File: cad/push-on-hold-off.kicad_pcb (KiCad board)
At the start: 2 copper layers, 11 parts, among them P1 CONN_01X04, P2 CONN_01X04, Q1 IRF7309IPBF, SW1 SW_PUSH_SMALL

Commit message: Do some placing and draw outline
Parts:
- moved R4 11.4 mm to (226.4, 111.2), turned to 180 degrees
- moved P1 7.50 mm to (218.4, 110.5), turned to 180 degrees
- moved C2 4.81 mm to (231.3, 111.1), turned to 0 degrees
- moved P2 3.47 mm to (236.2, 102.9)
- moved R1 3.00 mm to (221.0, 106.0), turned to 270 degrees
- moved R3 2.24 mm to (232.0, 102.0)
- moved R2 2.00 mm to (223.0, 106.0)
- moved SW1 1.70 mm to (227.3, 106.7)
- moved D1 1.17 mm to (226.4, 102.0)
- moved C1 1.06 mm to (222.4, 102.0)
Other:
- board outline added: 22.9 x 12.7 mm
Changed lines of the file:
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@@
     (links 27)
     (no_connects 27)
-    (area 0 0 0 0)
+    (area 215.824999 100.254999 238.835001 113.105001)
     (thickness 1.6)
-    (drawings 0)
+    (drawings 8)
     (tracks 0)
     (zones 0)
@@
   (layers
     (0 F.Cu signal)
-    (31 B.Cu signal)
+    (31 B.Cu signal hide)
     (32 B.Adhes user)
     (33 F.Adhes user)
@@
     (pad_to_mask_clearance 0.2)
     (aux_axis_origin 0 0)
-    (visible_elements FFFFFF7F)
+    (visible_elements FFFF7F7F)
     (pcbplotparams
       (layerselection 0x00030_80000001)
@@
   )
   (module Capacitors_SMD.pretty:C_0603_HandSoldering (layer F.Cu)
-    (at 222 103 180)
+    (at 222.36 102 180)
     (descr "Capacitor SMD 0603, hand soldering")
     (tags "capacitor 0603")
     (attr smd)
-    (fp_text reference C1 (at 0 -1.9 180) (layer F.SilkS)
-      (effects (font (size 1 1) (thickness 0.15)))
-    )
-    (fp_text value 1uF (at 0 1.9 180) (layer F.Fab)
+    (fp_text reference C1 (at 0.07 -1.64 180) (layer F.SilkS)
+      (effects (font (size 1 1) (thickness 0.15)))
+    )
+    (fp_text value 1uF (at -0.1 -1.51 180) (layer F.Fab)
       (effects (font (size 1 1) (thickness 0.15)))
     )
@@
   )
   (module Diodes_SMD.pretty:SOD-323 (layer F.Cu)
-    (at 227 103)
+    (at 226.39 102)
     (descr SOD-323)
     (tags SOD-323)
     (attr smd)
-    (fp_text reference D1 (at 0 -1.85) (layer F.SilkS)
+    (fp_text reference D1 (at 0.03 1.65) (layer F.SilkS)
       (effects (font (size 1 1) (thickness 0.15)))
     )
@@
     (tags "SOIC 1.27")
     (attr smd)
-    (fp_text reference Q1 (at 0 -3.68) (layer F.SilkS)
-      (effects (font (size 1 1) (thickness 0.15)))
-    )
-    (fp_text value IRF7309IPBF (at 0 3.68) (layer F.Fab)
+    (fp_text reference Q1 (at -6 -2) (layer F.SilkS)
+      (effects (font (size 1 1) (thickness 0.15)))
+    )
+    (fp_text value IRF7309IPBF (at 0.02 3.95) (layer F.Fab)
       (effects (font (size 1 1) (thickness 0.15)))
     )
@@
   )
   (module Resistors_SMD.pretty:R_0603_HandSoldering (layer F.Cu)
-    (at 221 109 90)
+    (at 221 106 270)
     (descr "Resistor SMD 0603, hand soldering")
     (tags "resistor 0603")
     (attr smd)
-    (fp_text reference R1 (at 0 -1.9 90) (layer F.SilkS)
-      (effects (font (size 1 1) (thickness 0.15)))
-    )
-    (fp_text value 10k (at 0 1.9 90) (layer F.Fab)
+    (fp_text reference R1 (at -3 -0.2 270) (layer F.SilkS)
+      (effects (font (size 1 1) (thickness 0.15)))
+    )
+    (fp_text value 10k (at 0 1.9 270) (layer F.Fab)
       (effects (font (size 1 1) (thickness 0.15)))
     )
@@
     (fp_line (start 0.5 0.675) (end -0.5 0.675) (layer F.SilkS) (width 0.15))
     (fp_line (start -0.5 -0.675) (end 0.5 -0.675) (layer F.SilkS) (width 0.15))
-    (pad 1 smd rect (at -1.1 0 90) (size 1.2 0.9) (layers F.Cu F.Paste F.Mask)
+    (pad 1 smd rect (at -1.1 0 270) (size 1.2 0.9) (layers F.Cu F.Paste F.Mask)
       (net 7 /Vin))
-    (pad 2 smd rect (at 1.1 0 90) (size 1.2 0.9) (layers F.Cu F.Paste F.Mask)
+    (pad 2 smd rect (at 1.1 0 270) (size 1.2 0.9) (layers F.Cu F.Paste F.Mask)
       (net 2 /Button))
     (model Resistors_SMD.3dshapes/R_0603_HandSoldering.wrl
@@
   )
   (module Resistors_SMD.pretty:R_0603_HandSoldering (layer F.Cu)
-    (at 223 108 270)
+    (at 223 106 270)
     (descr "Resistor SMD 0603, hand soldering")
     (tags "resistor 0603")
     (attr smd)
-    (fp_text reference R2 (at 0 -1.9 270) (layer F.SilkS)
-      (effects (font (size 1 1) (thickness 0.15)))
-    )
-    (fp_text value 100k (at 0 1.9 270) (layer F.Fab)
+    (fp_text reference R2 (at 3 0 270) (layer F.SilkS)
+      (effects (font (size 1 1) (thickness 0.15)))
+    )
+    (fp_text value 100k (at 0.91 1.77 270) (layer F.Fab)
       (effects (font (size 1 1) (thickness 0.15)))
     )
@@
   )
   (module Resistors_SMD.pretty:R_0603_HandSoldering (layer F.Cu)
-    (at 234 103)
+    (at 232 102)
     (descr "Resistor SMD 0603, hand soldering")
     (tags "resistor 0603")
     (attr smd)
-    (fp_text reference R3 (at 0 -1.9) (layer F.SilkS)
+    (fp_text reference R3 (at 0.35 1.67) (layer F.SilkS)
       (effects (font (size 1 1) (thickness 0.15)))
     )
@@
   )
   (module Resistors_SMD.pretty:R_0603_HandSoldering (layer F.Cu)
-    (at 237 107 90)
+    (at 226.43 111.15 180)
     (descr "Resistor SMD 0603, hand soldering")
     (tags "resistor 0603")
     (attr smd)
-    (fp_text reference R4 (at 0 -1.9 90) (layer F.SilkS)
-      (effects (font (size 1 1) (thickness 0.15)))
-    )
-    (fp_text value 100k (at 0 1.9 90) (layer F.Fab)
+    (fp_text reference R4 (at -0.4 -1.43 180) (layer F.SilkS)
+      (effects (font (size 1 1) (thickness 0.15)))
+    )
+    (fp_text value 100k (at 0 1.9 180) (layer F.Fab)
       (effects (font (size 1 1) (thickness 0.15)))
     )
@@
     (fp_line (start 0.5 0.675) (end -0.5 0.675) (layer F.SilkS) (width 0.15))
     (fp_line (start -0.5 -0.675) (end 0.5 -0.675) (layer F.SilkS) (width 0.15))
-    (pad 1 smd rect (at -1.1 0 90) (size 1.2 0.9) (layers F.Cu F.Paste F.Mask)
+    (pad 1 smd rect (at -1.1 0 180) (size 1.2 0.9) (layers F.Cu F.Paste F.Mask)
       (net 4 /Vout))
-    (pad 2 smd rect (at 1.1 0 90) (size 1.2 0.9) (layers F.Cu F.Paste F.Mask)
+    (pad 2 smd rect (at 1.1 0 180) (size 1.2 0.9) (layers F.Cu F.Paste F.Mask)
       (net 5 "Net-(D1-Pad2)"))
     (model Resistors_SMD.3dshapes/R_0603_HandSoldering.wrl
@@
   )
   (module Buttons_Switches_SMD.pretty:SW_SPST_EVPBF (layer B.Cu)
-    (at 229 107)
+    (at 227.33 106.68)
     (descr "Light Touch Switch")
     (attr smd)
@@
   )
   (module Pin_Headers.pretty:Pin_Header_Straight_1x04 (layer F.Cu)
-    (at 218 103)
+    (at 218.44 110.49 180)
     (descr "Through hole pin header")
     (tags "pin header")
-    (fp_text reference P1 (at 0 -5.1) (layer F.SilkS)
-      (effects (font (size 1 1) (thickness 0.15)))
-    )
-    (fp_text value CONN_01X04 (at 0 -3.1) (layer F.Fab)
+    (fp_text reference P1 (at 2.07 1.93 270) (layer F.SilkS)
+      (effects (font (size 1 1) (thickness 0.15)))
+    )
+    (fp_text value CONN_01X04 (at 0 -3.1 180) (layer F.Fab)
       (effects (font (size 1 1) (thickness 0.15)))
     )
@@
     (fp_line (start -1.55 0) (end -1.55 -1.55) (layer F.SilkS) (width 0.15))
     (fp_line (start -1.55 -1.55) (end 1.55 -1.55) (layer F.SilkS) (width 0.15))
-    (pad 1 thru_hole rect (at 0 0) (size 2.032 1.7272) (drill 1.016) (layers *.Cu *.Mask F.SilkS)
-      (net 6 GND))
-    (pad 2 thru_hole oval (at 0 2.54) (size 2.032 1.7272) (drill 1.016) (layers *.Cu *.Mask F.SilkS)
-      (net 6 GND))
-    (pad 3 thru_hole oval (at 0 5.08) (size 2.032 1.7272) (drill 1.016) (layers *.Cu *.Mask F.SilkS)
-      (net 2 /Button))
-    (pad 4 thru_hole oval (at 0 7.62) (size 2.032 1.7272) (drill 1.016) (layers *.Cu *.Mask F.SilkS)
+    (pad 1 thru_hole rect (at 0 0 180) (size 2.032 1.7272) (drill 1.016) (layers *.Cu *.Mask F.SilkS)
+      (net 6 GND))
+    (pad 2 thru_hole oval (at 0 2.54 180) (size 2.032 1.7272) (drill 1.016) (layers *.Cu *.Mask F.SilkS)
+      (net 6 GND))
+    (pad 3 thru_hole oval (at 0 5.08 180) (size 2.032 1.7272) (drill 1.016) (layers *.Cu *.Mask F.SilkS)
+      (net 2 /Button))
+    (pad 4 thru_hole oval (at 0 7.62 180) (size 2.032 1.7272) (drill 1.016) (layers *.Cu *.Mask F.SilkS)
       (net 7 /Vin))
     (model Pin_Headers.3dshapes/Pin_Header_Straight_1x04.wrl
@@
   )
   (module Pin_Headers.pretty:Pin_Header_Straight_1x04 (layer F.Cu)
-    (at 239.67 103.21)
+    (at 236.22 102.87)
     (descr "Through hole pin header")
     (tags "pin header")
-    (fp_text reference P2 (at 0 -5.1) (layer F.SilkS)
+    (fp_text reference P2 (at -2.07 1.07 90) (layer F.SilkS)
       (effects (font (size 1 1) (thickness 0.15)))
     )
@@
   )
   (module Capacitors_SMD.pretty:C_0603_HandSoldering (layer F.Cu)
-    (at 235 108 270)
+    (at 231.32 111.09)
     (descr "Capacitor SMD 0603, hand soldering")
     (tags "capacitor 0603")
     (attr smd)
-    (fp_text reference C2 (at 0 -1.9 270) (layer F.SilkS)
-      (effects (font (size 1 1) (thickness 0.15)))
-    )
-    (fp_text value 10uF (at 0 1.9 270) (layer F.Fab)
+    (fp_text reference C2 (at 0 1.45) (layer F.SilkS)
+      (effects (font (size 1 1) (thickness 0.15)))
+    )
+    (fp_text value 10uF (at 0 1.9) (layer F.Fab)
       (effects (font (size 1 1) (thickness 0.15)))
     )
@@
     (fp_line (start -0.35 -0.6) (end 0.35 -0.6) (layer F.SilkS) (width 0.15))
     (fp_line (start 0.35 0.6) (end -0.35 0.6) (layer F.SilkS) (width 0.15))
-    (pad 1 smd rect (at -0.95 0 270) (size 1.2 0.75) (layers F.Cu F.Paste F.Mask)
+    (pad 1 smd rect (at -0.95 0) (size 1.2 0.75) (layers F.Cu F.Paste F.Mask)
       (net 3 "Net-(C2-Pad1)"))
-    (pad 2 smd rect (at 0.95 0 270) (size 1.2 0.75) (layers F.Cu F.Paste F.Mask)
+    (pad 2 smd rect (at 0.95 0) (size 1.2 0.75) (layers F.Cu F.Paste F.Mask)
       (net 4 /Vout))
     (model Capacitors_SMD.3dshapes/C_0603_HandSoldering.wrl
@@
     )
   )
+  (gr_line (start 237.49 100.33) (end 217.17 100.33) (angle 90) (layer Edge.Cuts) (width 0.15))
+  (gr_line (start 238.76 101.6) (end 237.49 100.33) (angle 90) (layer Edge.Cuts) (width 0.15))
+  (gr_line (start 238.76 111.76) (end 238.76 101.6) (angle 90) (layer Edge.Cuts) (width 0.15))
+  (gr_line (start 237.49 113.03) (end 238.76 111.76) (angle 90) (layer Edge.Cuts) (width 0.15))
+  (gr_line (start 217.17 113.03) (end 237.49 113.03) (angle 90) (layer Edge.Cuts) (width 0.15))
+  (gr_line (start 215.9 111.76) (end 217.17 113.03) (angle 90) (layer Edge.Cuts) (width 0.15))
+  (gr_line (start 215.9 101.6) (end 215.9 111.76) (angle 90) (layer Edge.Cuts) (width 0.15))
+  (gr_line (start 217.17 100.33) (end 215.9 101.6) (angle 90) (layer Edge.Cuts) (width 0.15))
 )

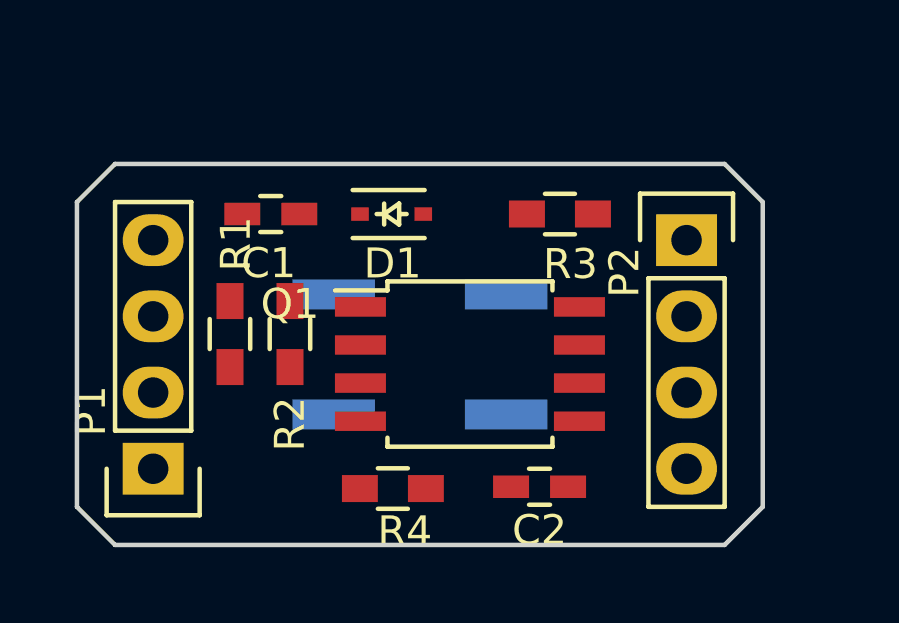
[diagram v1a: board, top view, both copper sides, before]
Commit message: Route most components
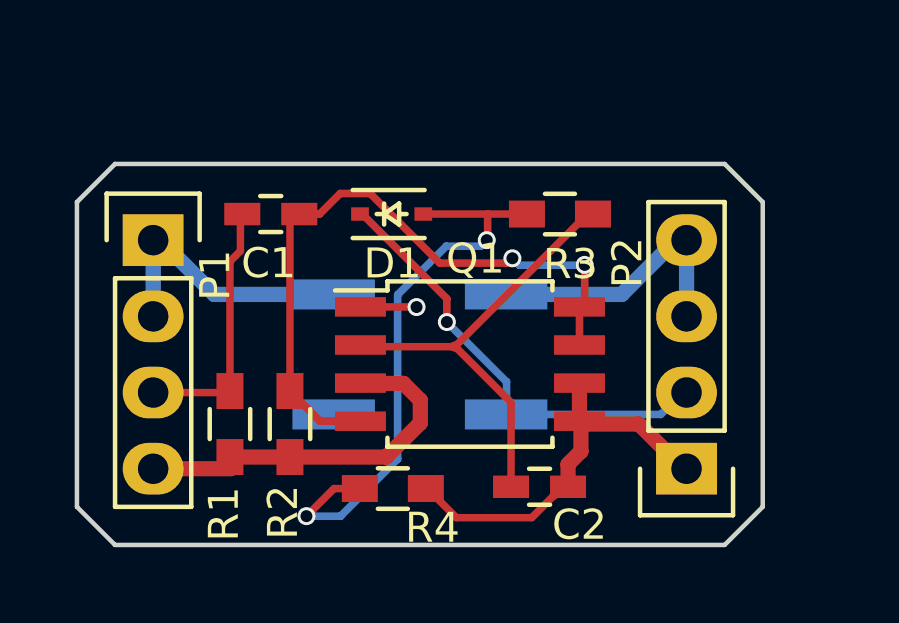
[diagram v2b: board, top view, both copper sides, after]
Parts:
- moved P1 7.62 mm to (218.4, 102.9), turned to 0 degrees
- moved P2 7.62 mm to (236.2, 110.5), turned to 180 degrees
- moved R1 3.00 mm to (221.0, 109.0), turned to 90 degrees
- moved R2 3.00 mm to (223.0, 109.0), turned to 90 degrees
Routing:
- net /Button: track 0.00 -> 23.9 mm, vias 0 -> 1
- net Net-(C1-Pad1): track 0.00 -> 22.9 mm, vias 0 -> 2
- net GND: track 0.00 -> 21.5 mm, vias 0 -> 1
- net Net-(D1-Pad2): track 0.00 -> 19.7 mm, vias 0 -> 2
- net Net-(C2-Pad1): track 0.00 -> 15.2 mm
- net /Vin: track 0.00 -> 13.6 mm
- net /Vout: track 0.00 -> 13.4 mm
- added copper zone on B.Cu, net GND
- added copper zone on F.Cu, net GND
